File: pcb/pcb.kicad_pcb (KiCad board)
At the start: 2 copper layers, 77.3 x 67 mm, 45 parts, among them CN1 Battery_Cell, Q1 AO3401A, Q2 AO3400A, U1 TPS63802DLAT, U2 USB-C 6PIN, U3 BQ24075RGTR, U4 ESP-32S DevBoard, U5 Water_Sensor, U6 Pump

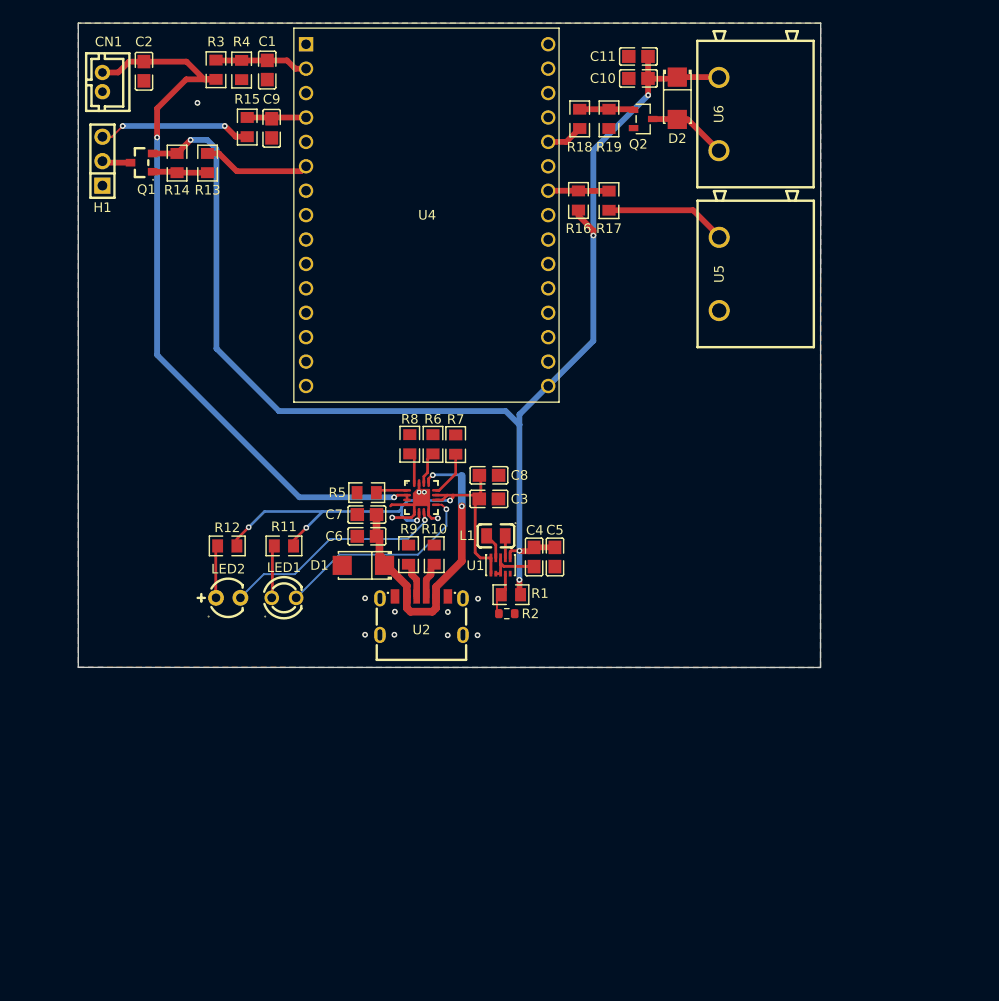
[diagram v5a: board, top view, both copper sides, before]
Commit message: Copied any model into the custom library to have full control of everything
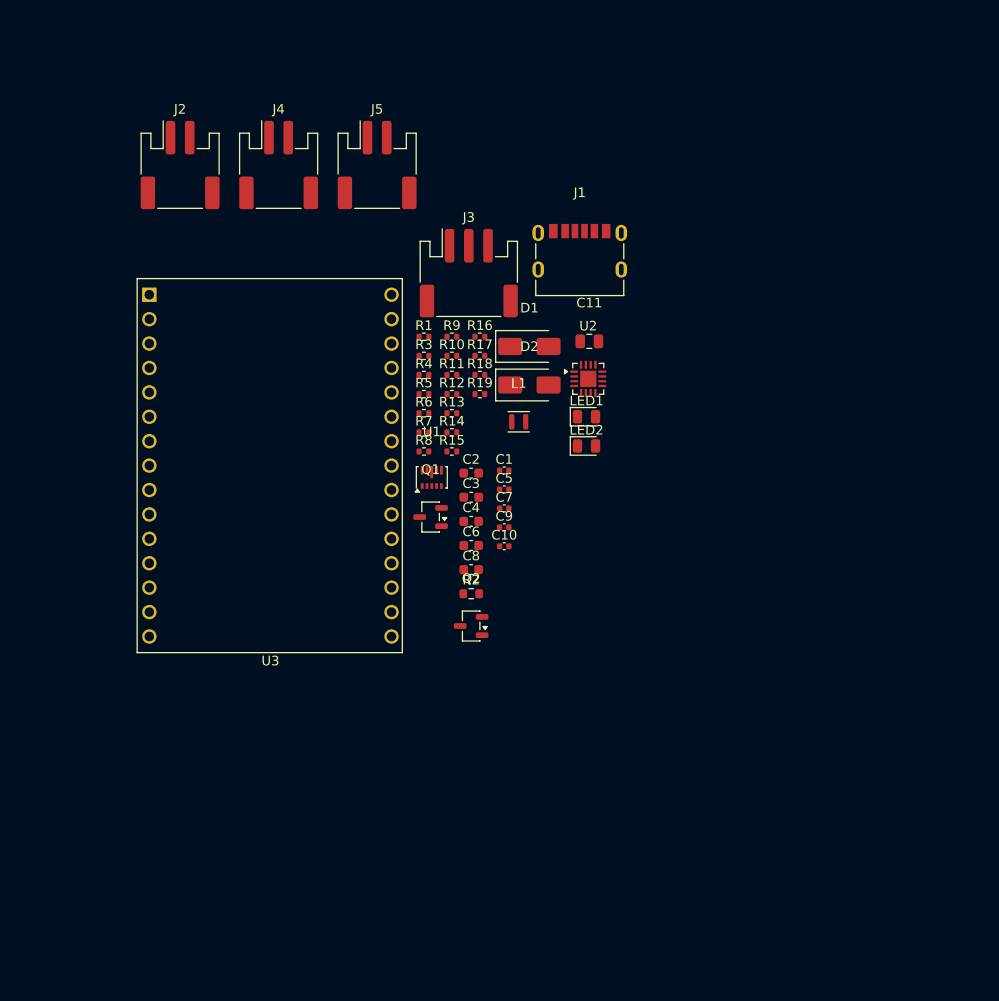
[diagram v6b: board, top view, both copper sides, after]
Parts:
- removed CN1: Battery_Cell, EasyEDA:CONN-TH_B2B-PH-K-S
- removed H1: Soil_Sensor, EasyEDA:HDR-TH_3P-P2.54-V-M_PZ254V-11-03P
- removed U4: ESP-32S DevBoard, custom:ESP-32S_USB-C_CH340_DevBoard
- removed U5: Water_Sensor, EasyEDA:CONN-TH_MX7620-7.62-02P-GN01-CU-S-A
- removed U6: Pump, EasyEDA:CONN-TH_MX7620-7.62-02P-GN01-CU-S-A
- added J1: USB-C, custom:USB_C_Receptacle_HX_TYPE-C-6P, F.Cu at (158.6, 76.8)
- added J2: Battery, custom:JST_PH_S2B-PH-SM4-TB_1x02-1MP_P2.00mm_Horizontal, F.Cu at (117.0, 68.0)
- added J3: Soil_Sensor, custom:JST_PH_S3B-PH-SM4-TB_1x03-1MP_P2.00mm_Horizontal, F.Cu at (147.0, 79.2)
- added J4: Pump, custom:JST_PH_S2B-PH-SM4-TB_1x02-1MP_P2.00mm_Horizontal, F.Cu at (127.2, 68.0)
- added J5: Water_Sensor, custom:JST_PH_S2B-PH-SM4-TB_1x02-1MP_P2.00mm_Horizontal, F.Cu at (137.5, 68.0)
- C1, C10, C5, C7, C9: footprint EasyEDA:C0805 -> custom:C_0402_1005Metric
- C11: value 47uF -> 100uF; footprint EasyEDA:C0805 -> custom:C_0805_2012Metric
- C2, C3, C4, C6, C8: footprint EasyEDA:C0805 -> custom:C_0603_1608Metric
- D1: value SMAJ5.0A -> SMAJ6.0A; footprint EasyEDA:SMA_L4.3-W2.6-LS5.2-RD -> custom:D_SMA
- D2: value Schottky 40V -> SS34; footprint EasyEDA:SMA_L4.3-W2.6-LS5.2-RD -> custom:D_SMA
- L1: footprint EasyEDA:IND-SMD_L2.0-W1.6-1 -> custom:L_Murata_DFE201610P
- LED1: value RED 2V -> Red; footprint EasyEDA:LED-TH_BD3.0-P2.54-FD -> custom:LED_0805_2012Metric
- LED2: value GREEN 2V -> Green; footprint EasyEDA:LED-TH_BD4.0-P2.54-FD -> custom:LED_0805_2012Metric
- Q1: footprint EasyEDA:SOT-23_L2.9-W1.3-P1.90-LS2.4-BR -> custom:SOT-23-3
- Q2: footprint EasyEDA:SOT-23-3_L2.9-W1.3-P1.90-LS2.4-BR -> custom:SOT-23-3
- R1, R10, R11, R12, R13, R14, R15, R16, R17, R18, R19, R3, R4, R5, R6, R7, R8, R9: footprint EasyEDA:R0805 -> custom:R_0402_1005Metric
- R2: footprint Resistor_SMD:R_0603_1608Metric -> custom:R_0603_1608Metric
- U1: value TPS63802DLAT -> TPS63802DLAR; footprint EasyEDA:VSON-10-HR_L3.0-W2.0-P0.50-BL_TI_DLA -> custom:Texas_VSON-HR-10_2x3mm_P0.5mm
- U2: value USB-C 6PIN -> BQ24075RGTR; footprint EasyEDA:USB-C-SMD_HX-TYPE-C-6PIN -> custom:QFN-16-1EP_3x3mm_P0.5mm_EP1.7x1.7mm
- U3: value BQ24075RGTR -> ESP-32S DevBoard; footprint EasyEDA:QFN-16_L3.0-W3.0-P0.50-TL-EP1.7 -> custom:ESP-32S_USB-C_CH340_DevBoard
- moved Q2 55.7 mm to (147.3, 115.9)
- moved C2 53.9 mm to (147.3, 100.0), turned to 0 degrees
- moved C10 50.6 mm to (150.7, 107.6), turned to 0 degrees
- moved C1 48.4 mm to (150.7, 99.8), turned to 0 degrees
- moved C9 48.1 mm to (150.7, 105.7), turned to 0 degrees
- moved Q1 47.6 mm to (143.1, 104.6), turned to 180 degrees
- moved LED2 40.5 mm to (159.3, 97.2)
- moved R14 40.0 mm to (145.3, 95.8), turned to 0 degrees
- moved R15 39.9 mm to (145.3, 97.8), turned to 0 degrees
- moved R4 37.0 mm to (142.4, 89.8), turned to 0 degrees
- moved R3 36.8 mm to (142.4, 87.8), turned to 0 degrees
- moved LED1 36.7 mm to (159.3, 94.2)
- moved R13 36.4 mm to (145.3, 93.8), turned to 0 degrees
- moved U3 35.3 mm to (113.8, 81.5)
- moved D2 33.6 mm to (153.3, 90.9), turned to 0 degrees
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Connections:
- LED1 pad 1: Net-(LED1-Pad1) -> Net-(U2-#CHG)
- LED1 pad 2: Net-(U3-#CHG) -> Net-(LED1-Pad2)
- LED2 pad 1: Net-(LED2-Pad1) -> Net-(U2-#PGOOD)
- LED2 pad 2: Net-(U3-#PGOOD) -> Net-(LED2-Pad2)
- R10 pad 1: Net-(U2-CC2) -> Net-(J1-CC2)
- R11 pad 1: Net-(LED1-Pad1) -> Net-(LED1-Pad2)
- R12 pad 1: Net-(LED2-Pad1) -> Net-(LED2-Pad2)
- R5 pad 2: Net-(U3-TS) -> Net-(U2-TS)
- R6 pad 2: Net-(U3-TMR) -> Net-(U2-TMR)
- R7 pad 2: Net-(U3-ILIM) -> Net-(U2-ILIM)
- R8 pad 2: Net-(U3-ISET) -> Net-(U2-ISET)
- R9 pad 1: Net-(U2-CC1) -> Net-(J1-CC1)
- U2 pad 13: GND -> VBUS
- U2 pad 14: GND -> Net-(U2-TMR)
- U2 pad 16: GND -> Net-(U2-ISET)
- U3 pad 1: Net-(U3-TS) -> unconnected-(U3-EN-Pad1)
- U3 pad 10: VIMM -> unconnected-(U3-D27-Pad10)
- U3 pad 11: VIMM -> unconnected-(U3-D14-Pad11)
- U3 pad 12: Net-(U3-ILIM) -> unconnected-(U3-D12-Pad12)
- U3 pad 13: VBUS -> unconnected-(U3-D13-Pad13)
- U3 pad 14: Net-(U3-TMR) -> GND
- U3 pad 15: GND -> unconnected-(U3-VIN-Pad15)
- U3 pad 16: Net-(U3-ISET) -> unconnected-(U3-D23-Pad16)
- U3 pad 17: GND -> unconnected-(U3-D22-Pad17)
- U3 pad 2: Net-(C2-Pad1) -> BAT_SENSE
- U3 pad 3: Net-(C2-Pad1) -> unconnected-(U3-VN-Pad3)
- U3 pad 4: GND -> SOIL_OUT
- U3 pad 5: GND -> unconnected-(U3-D35-Pad5)
- U3 pad 6: VIMM -> ~{SOIL_ON}
- U3 pad 7: Net-(U3-#PGOOD) -> unconnected-(U3-D33-Pad7)
- U3 pad 8: GND -> unconnected-(U3-D25-Pad8)
- U3 pad 9: Net-(U3-#CHG) -> unconnected-(U3-D26-Pad9)
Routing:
- net +3.3V: track 141.3 -> 0.00 mm, vias 5 -> 0
- net Net-(C2-Pad1): track 78.8 -> 0.00 mm, vias 2 -> 0
- net VIMM: track 52.5 -> 0.00 mm, vias 4 -> 0
- net VBUS: track 33.0 -> 0.00 mm, vias 2 -> 0
- net Net-(U3-#PGOOD): track 23.5 -> 0.00 mm, vias 1 -> 0
- net Net-(U3-#CHG): track 21.8 -> 0.00 mm, vias 1 -> 0
- net GND: track 17.6 -> 0.00 mm, vias 13 -> 0
- net Net-(J3-Pad3): track 16.0 -> 0.00 mm, vias 2 -> 0
- net Net-(J5-Pad2): track 12.7 -> 0.00 mm
- net ~{SOIL_ON}: track 11.2 -> 0.00 mm
- net BAT_SENSE: track 9.74 -> 0.00 mm
- net Net-(Q2-D): track 8.25 -> 0.00 mm
- net WATER_OUT: track 6.38 -> 0.00 mm
- net SOIL_OUT: track 6.23 -> 0.00 mm
- net Net-(Q1-G): track 5.75 -> 0.00 mm
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- removed copper zone on B.Cu, net GND
- removed copper zone on F.Cu, net GND
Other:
- board outline removed

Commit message: Added new keepout zones etc for the U3
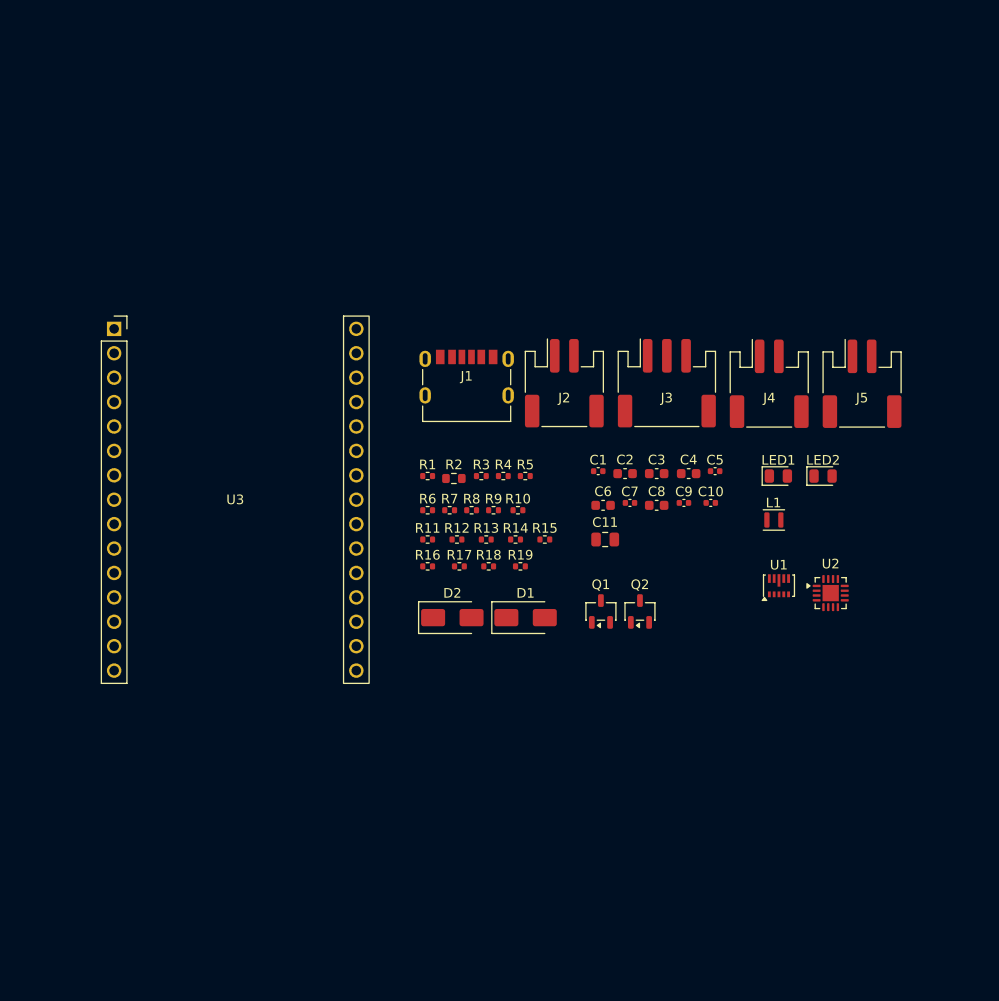
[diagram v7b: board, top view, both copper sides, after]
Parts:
- moved J4 55.9 mm to (178.3, 90.7)
- moved J5 55.4 mm to (188.0, 90.7)
- moved J2 46.0 mm to (157.0, 90.7)
- moved U1 37.8 mm to (179.3, 111.8)
- moved U2 33.7 mm to (184.7, 112.5)
- moved L1 28.4 mm to (178.8, 104.9)
- moved D1 28.2 mm to (152.9, 115.1)
- moved D2 25.5 mm to (145.3, 115.1)
- moved LED2 24.8 mm to (183.9, 100.3)
- moved R16 24.5 mm to (142.8, 109.7)
- moved J3 23.6 mm to (167.6, 90.7)
- moved C4 23.2 mm to (169.9, 100.1)
- moved C5 22.0 mm to (172.7, 99.8)
- moved R17 22.0 mm to (146.1, 109.7)
- moved C10 22.0 mm to (172.2, 103.1)
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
